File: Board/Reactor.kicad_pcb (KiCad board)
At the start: 2 copper layers, 72.4 x 77.1 mm, 26 parts, among them P1 CONN_02X13, P2 USER_PORT, P3 CONN_01X13, P4 LA_PWR, P5 USB_OTG, P6 DEBUG, U1 usb1232h, U2 PCF8574

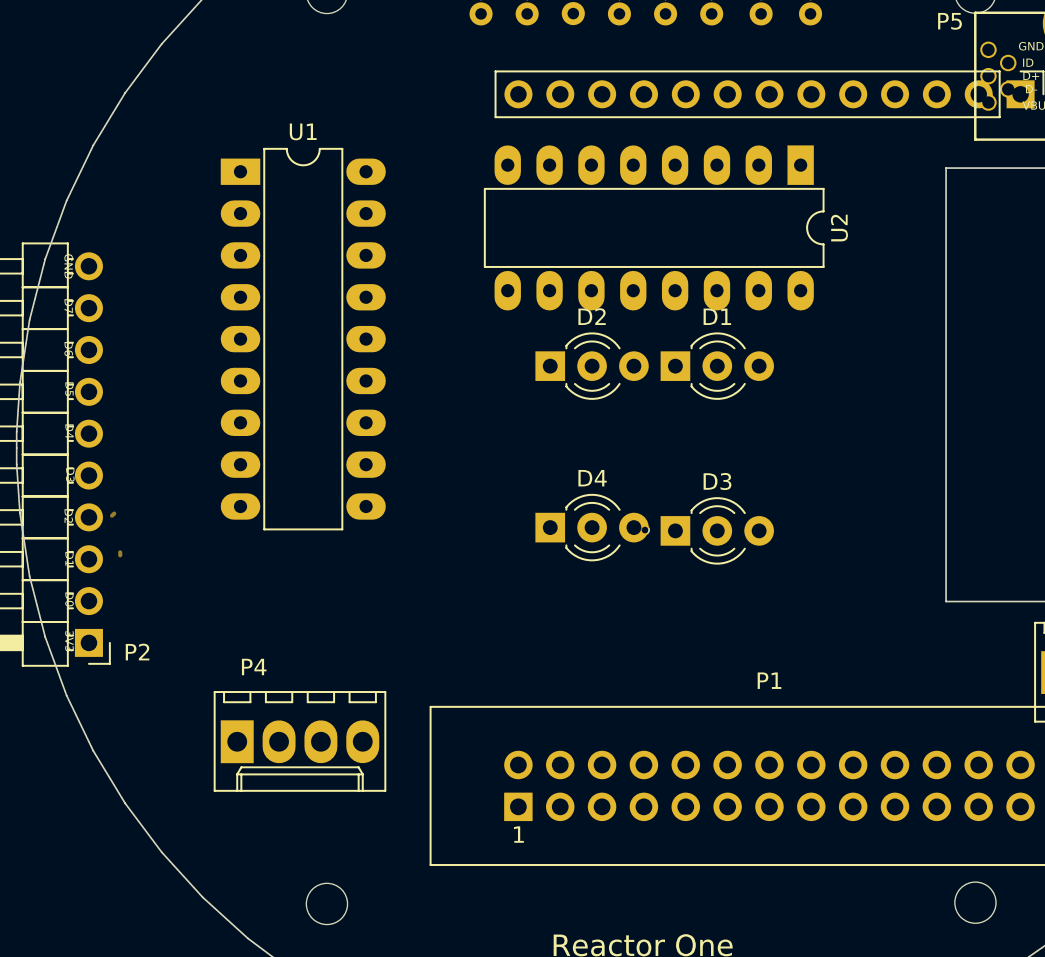
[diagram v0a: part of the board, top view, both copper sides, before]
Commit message: Moved to a template FastSharedBuffer.
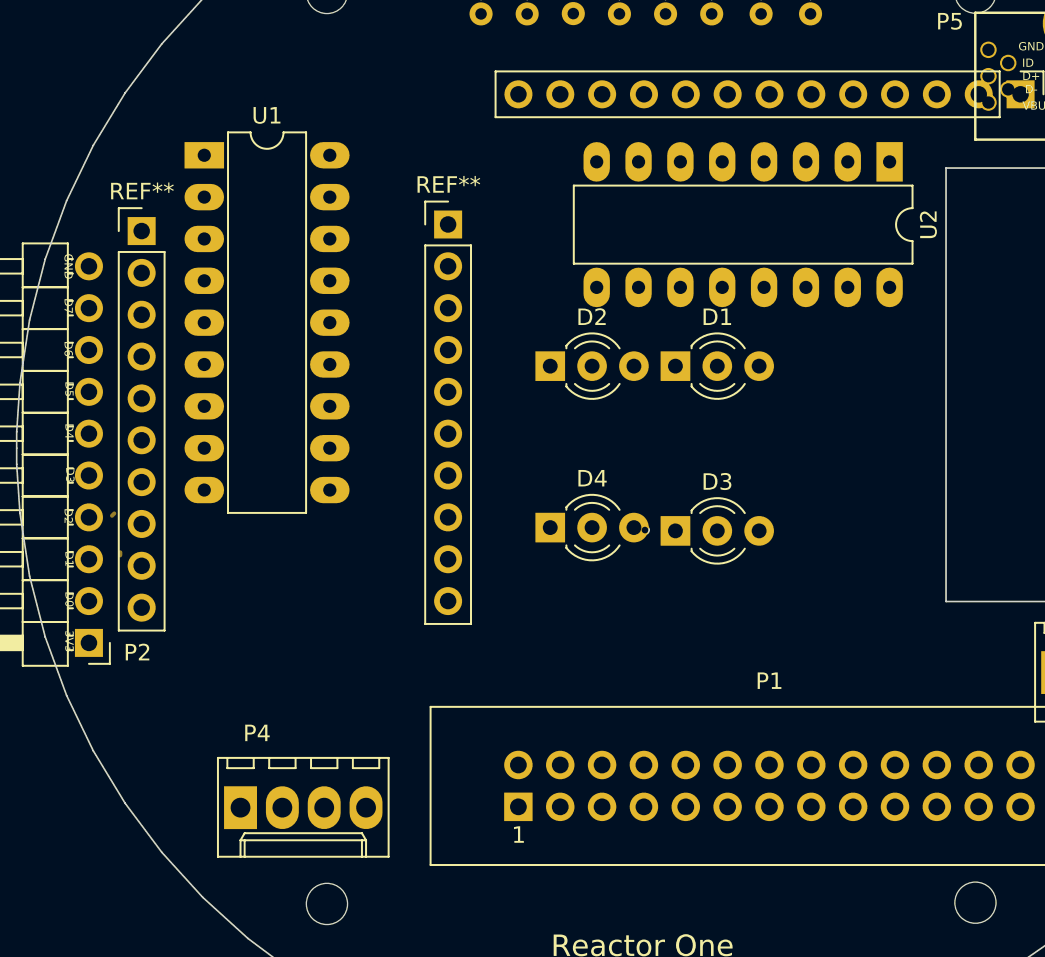
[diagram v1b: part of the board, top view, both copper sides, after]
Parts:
- added REF**: Pin_Header_Straight_1x10_Pitch2.54mm, Pin_Headers_new:Pin_Header_Straight_1x10_Pitch2.54mm, F.Cu at (146.2, 81.9)
- added REF**: Pin_Header_Straight_1x10_Pitch2.54mm, Pin_Headers_new:Pin_Header_Straight_1x10_Pitch2.54mm, F.Cu at (127.6, 82.3)
- moved U2 5.40 mm to (173.0, 78.1)
- moved P4 4.00 mm to (133.6, 117.3)
- moved U1 2.42 mm to (131.4, 77.7)
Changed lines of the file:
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@@
     (tracks 16)
     (zones 0)
-    (modules 26)
+    (modules 28)
     (nets 54)
   )
@@
   )
   (module Connectors_Molex:Molex_KK-6410-04_04x2.54mm_Straight (layer F.Cu)
-    (at 133.39 113.27)
+    (at 133.59 117.27)
     (descr "Connector Headers with Friction Lock, 22-27-2041, http://www.molex.com/pdm_docs/sd/022272021_sd.pdf")
     (tags "connector molex kk_6410 22-27-2041")
@@
   )
   (module Housings_DIP:DIP-18_W7.62mm_LongPads (layer F.Cu)
-    (at 133.59 78.67)
+    (at 131.39 77.67)
     (descr "18-lead dip package, row spacing 7.62 mm (300 mils), LongPads")
     (tags "DIL DIP PDIP 2.54mm 7.62mm 300mil LongPads")
@@
   )
   (module Housings_DIP:DIP-16_W7.62mm_LongPads (layer F.Cu)
-    (at 167.59 78.27 270)
+    (at 172.99 78.07 270)
     (descr "16-lead dip package, row spacing 7.62 mm (300 mils), LongPads")
     (tags "DIL DIP PDIP 2.54mm 7.62mm 300mil LongPads")
@@
     )
   )
-  (gr_line (start 129.99 107.07) (end 129.99 74.87) (angle 90) (layer Cmts.User) (width 0.2))
-  (gr_line (start 144.99 107.07) (end 129.99 107.07) (angle 90) (layer Cmts.User) (width 0.2))
-  (gr_line (start 144.99 74.87) (end 144.99 107.07) (angle 90) (layer Cmts.User) (width 0.2))
-  (gr_line (start 129.99 74.87) (end 144.79 74.87) (angle 90) (layer Cmts.User) (width 0.2))
+  (module Pin_Headers_new:Pin_Header_Straight_1x10_Pitch2.54mm (layer F.Cu)
+    (at 146.19 81.87)
+    (descr "Through hole straight pin header, 1x10, 2.54mm pitch, single row")
+    (tags "Through hole pin header THT 1x10 2.54mm single row")
+    (fp_text reference REF** (at 0 -2.39) (layer F.SilkS)
+      (effects (font (size 1 1) (thickness 0.15)))
+    )
+    (fp_text value Pin_Header_Straight_1x10_Pitch2.54mm (at 0 25.25) (layer F.Fab)
+      (effects (font (size 1 1) (thickness 0.15)))
+    )
+    (fp_line (start -1.27 -1.27) (end -1.27 24.13) (layer F.Fab) (width 0.1))
+    (fp_line (start -1.27 24.13) (end 1.27 24.13) (layer F.Fab) (width 0.1))
+    (fp_line (start 1.27 24.13) (end 1.27 -1.27) (layer F.Fab) (width 0.1))
+    (fp_line (start 1.27 -1.27) (end -1.27 -1.27) (layer F.Fab) (width 0.1))
+    (fp_line (start -1.39 1.27) (end -1.39 24.25) (layer F.SilkS) (width 0.12))
+    (fp_line (start -1.39 24.25) (end 1.39 24.25) (layer F.SilkS) (width 0.12))
+    (fp_line (start 1.39 24.25) (end 1.39 1.27) (layer F.SilkS) (width 0.12))
+    (fp_line (start 1.39 1.27) (end -1.39 1.27) (layer F.SilkS) (width 0.12))
+    (fp_line (start -1.39 0) (end -1.39 -1.39) (layer F.SilkS) (width 0.12))
+    (fp_line (start -1.39 -1.39) (end 0 -1.39) (layer F.SilkS) (width 0.12))
+    (fp_line (start -1.6 -1.6) (end -1.6 24.4) (layer F.CrtYd) (width 0.05))
+    (fp_line (start -1.6 24.4) (end 1.6 24.4) (layer F.CrtYd) (width 0.05))
+    (fp_line (start 1.6 24.4) (end 1.6 -1.6) (layer F.CrtYd) (width 0.05))
+    (fp_line (start 1.6 -1.6) (end -1.6 -1.6) (layer F.CrtYd) (width 0.05))
+    (pad 1 thru_hole rect (at 0 0) (size 1.7 1.7) (drill 1) (layers *.Cu *.Mask))
+    (pad 2 thru_hole oval (at 0 2.54) (size 1.7 1.7) (drill 1) (layers *.Cu *.Mask))
+    (pad 3 thru_hole oval (at 0 5.08) (size 1.7 1.7) (drill 1) (layers *.Cu *.Mask))
+    (pad 4 thru_hole oval (at 0 7.62) (size 1.7 1.7) (drill 1) (layers *.Cu *.Mask))
+    (pad 5 thru_hole oval (at 0 10.16) (size 1.7 1.7) (drill 1) (layers *.Cu *.Mask))
+    (pad 6 thru_hole oval (at 0 12.7) (size 1.7 1.7) (drill 1) (layers *.Cu *.Mask))
+    (pad 7 thru_hole oval (at 0 15.24) (size 1.7 1.7) (drill 1) (layers *.Cu *.Mask))
+    (pad 8 thru_hole oval (at 0 17.78) (size 1.7 1.7) (drill 1) (layers *.Cu *.Mask))
+    (pad 9 thru_hole oval (at 0 20.32) (size 1.7 1.7) (drill 1) (layers *.Cu *.Mask))
+    (pad 10 thru_hole oval (at 0 22.86) (size 1.7 1.7) (drill 1) (layers *.Cu *.Mask))
+    (model Pin_Headers.3dshapes/Pin_Header_Straight_1x10_Pitch2.54mm.wrl
+      (at (xyz 0 -0.45 0))
+      (scale (xyz 1 1 1))
+      (rotate (xyz 0 0 90))
+    )
+  )
+  (module Pin_Headers_new:Pin_Header_Straight_1x10_Pitch2.54mm (layer F.Cu)
+    (at 127.59 82.27)
+    (descr "Through hole straight pin header, 1x10, 2.54mm pitch, single row")
+    (tags "Through hole pin header THT 1x10 2.54mm single row")
+    (fp_text reference REF** (at 0 -2.39) (layer F.SilkS)
+      (effects (font (size 1 1) (thickness 0.15)))
+    )
+    (fp_text value Pin_Header_Straight_1x10_Pitch2.54mm (at 0 25.25) (layer F.Fab)
+      (effects (font (size 1 1) (thickness 0.15)))
+    )
+    (fp_line (start -1.27 -1.27) (end -1.27 24.13) (layer F.Fab) (width 0.1))
+    (fp_line (start -1.27 24.13) (end 1.27 24.13) (layer F.Fab) (width 0.1))
+    (fp_line (start 1.27 24.13) (end 1.27 -1.27) (layer F.Fab) (width 0.1))
+    (fp_line (start 1.27 -1.27) (end -1.27 -1.27) (layer F.Fab) (width 0.1))
+    (fp_line (start -1.39 1.27) (end -1.39 24.25) (layer F.SilkS) (width 0.12))
+    (fp_line (start -1.39 24.25) (end 1.39 24.25) (layer F.SilkS) (width 0.12))
+    (fp_line (start 1.39 24.25) (end 1.39 1.27) (layer F.SilkS) (width 0.12))
+    (fp_line (start 1.39 1.27) (end -1.39 1.27) (layer F.SilkS) (width 0.12))
+    (fp_line (start -1.39 0) (end -1.39 -1.39) (layer F.SilkS) (width 0.12))
+    (fp_line (start -1.39 -1.39) (end 0 -1.39) (layer F.SilkS) (width 0.12))
+    (fp_line (start -1.6 -1.6) (end -1.6 24.4) (layer F.CrtYd) (width 0.05))
+    (fp_line (start -1.6 24.4) (end 1.6 24.4) (layer F.CrtYd) (width 0.05))
+    (fp_line (start 1.6 24.4) (end 1.6 -1.6) (layer F.CrtYd) (width 0.05))
+    (fp_line (start 1.6 -1.6) (end -1.6 -1.6) (layer F.CrtYd) (width 0.05))
+    (pad 1 thru_hole rect (at 0 0) (size 1.7 1.7) (drill 1) (layers *.Cu *.Mask))
+    (pad 2 thru_hole oval (at 0 2.54) (size 1.7 1.7) (drill 1) (layers *.Cu *.Mask))
+    (pad 3 thru_hole oval (at 0 5.08) (size 1.7 1.7) (drill 1) (layers *.Cu *.Mask))
+    (pad 4 thru_hole oval (at 0 7.62) (size 1.7 1.7) (drill 1) (layers *.Cu *.Mask))
+    (pad 5 thru_hole oval (at 0 10.16) (size 1.7 1.7) (drill 1) (layers *.Cu *.Mask))
+    (pad 6 thru_hole oval (at 0 12.7) (size 1.7 1.7) (drill 1) (layers *.Cu *.Mask))
+    (pad 7 thru_hole oval (at 0 15.24) (size 1.7 1.7) (drill 1) (layers *.Cu *.Mask))
+    (pad 8 thru_hole oval (at 0 17.78) (size 1.7 1.7) (drill 1) (layers *.Cu *.Mask))
+    (pad 9 thru_hole oval (at 0 20.32) (size 1.7 1.7) (drill 1) (layers *.Cu *.Mask))
+    (pad 10 thru_hole oval (at 0 22.86) (size 1.7 1.7) (drill 1) (layers *.Cu *.Mask))
+    (model Pin_Headers.3dshapes/Pin_Header_Straight_1x10_Pitch2.54mm.wrl
+      (at (xyz 0 -0.45 0))
+      (scale (xyz 1 1 1))
+      (rotate (xyz 0 0 90))
+    )
+  )
+  (gr_line (start 148.99 74.67) (end 126.59 74.67) (angle 90) (layer Cmts.User) (width 0.2))
+  (gr_line (start 148.99 113.07) (end 148.99 74.67) (angle 90) (layer Cmts.User) (width 0.2))
+  (gr_line (start 126.59 113.07) (end 148.99 113.07) (angle 90) (layer Cmts.User) (width 0.2))
+  (gr_line (start 126.59 74.67) (end 126.59 113.07) (angle 90) (layer Cmts.User) (width 0.2))
   (gr_text CLK (at 178.49 118.72) (layer B.SilkS)
     (effects (font (size 0.5 0.5) (thickness 0.1)) (justify mirror))

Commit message: - board laid out (draft).
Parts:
- removed ? (x4): , Mounting_Holes:MountingHole_2.5mm
- removed P4: LA_PWR, Connectors_Molex:Molex_KK-6410-04_04x2.54mm_Straight
- removed REF** (x2): MountingHole_2.2mm_M2_DIN965_Pad, Mounting_Holes:MountingHole_2.2mm_M2_DIN965_Pad
- removed REF** (x2): Pin_Header_Straight_1x10_Pitch2.54mm, Pin_Headers_new:Pin_Header_Straight_1x10_Pitch2.54mm
- D1, D2, D3, D4: value LED_Dual_AAC -> LED_Dual_CAC; footprint LEDs_new:LED_D3.0mm-3 -> sip:SIP3
- U1: value usb1232h -> AdafruitFT232H; footprint Housings_DIP:DIP-18_W7.62mm_LongPads -> ReactorProject:AdafruitFT232h
- moved R2 41.9 mm to (162.0, 102.9), turned to 0 degrees
- moved R4 41.8 mm to (151.0, 103.3), turned to 0 degrees
- moved U1 41.3 mm to (149.8, 114.7), turned to 90 degrees
- moved R5 37.8 mm to (169.6, 97.9), turned to 180 degrees
- moved R7 37.0 mm to (158.6, 97.9), turned to 180 degrees
- moved R3 31.9 mm to (150.8, 93.3), turned to 0 degrees
- moved R1 31.8 mm to (162.2, 93.3), turned to 0 degrees
- moved R8 26.5 mm to (158.6, 87.9), turned to 180 degrees
- moved R6 20.5 mm to (162.0, 87.9), turned to 0 degrees
- moved U2 17.6 mm to (167.8, 61.3)
- moved P5 8.44 mm to (173.4, 67.9)
- moved D2 2.60 mm to (155.0, 90.5)
- moved D1 2.60 mm to (162.6, 90.5)
- moved D4 2.41 mm to (154.8, 100.5)
- moved D3 2.40 mm to (162.4, 100.5)
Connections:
- net /PA19 renamed Net-(P1-Pad16)
- D1 pad 2: Net-(D1-Pad2) -> /3v3
- D1 pad 3: +5V -> Net-(D1-Pad3)
- D2 pad 2: Net-(D2-Pad2) -> /3v3
- D2 pad 3: +5V -> Net-(D2-Pad3)
- D3 pad 2: Net-(D3-Pad2) -> /3v3
- D3 pad 3: +5V -> Net-(D3-Pad3)
- D4 pad 2: Net-(D4-Pad2) -> /3v3
- D4 pad 3: +5V -> Net-(D4-Pad3)
- P1 pad 12: /3v3 -> /D7
- P1 pad 18: /3v3 -> /D7
- P1 pad 21: /3v3 -> /D6
- P1 pad 25: +5V -> /GND
- P1 pad 7: /3v3 -> /D6
- P2 pad 1: +5V -> /GND
- P2 pad 8: /3v3 -> /D6
- P2 pad 9: /3v3 -> /D7
- P3 pad 1: +5V -> /5V
- P3 pad 2: +5V -> /GND
- P5 pad 1: +5V -> /5V
- P5 pad 5: +5V -> /GND
- P6 pad 1: +5V -> Net-(P6-Pad1)
- R1 pad 1: Net-(R1-Pad1) -> Net-(D1-Pad3)
- R1 pad 2: Net-(D3-Pad1) -> Net-(R1-Pad2)
- R2 pad 1: Net-(R2-Pad1) -> Net-(D3-Pad1)
- R2 pad 2: Net-(D3-Pad2) -> Net-(R2-Pad2)
- R3 pad 1: Net-(R3-Pad1) -> Net-(D2-Pad1)
- R3 pad 2: Net-(D4-Pad1) -> Net-(R3-Pad2)
- R4 pad 1: Net-(R4-Pad1) -> Net-(D4-Pad1)
- R4 pad 2: Net-(D4-Pad2) -> Net-(R4-Pad2)
- R5 pad 1: Net-(R5-Pad1) -> Net-(D3-Pad3)
- R5 pad 2: Net-(D1-Pad1) -> Net-(R5-Pad2)
- R6 pad 1: Net-(R6-Pad1) -> Net-(D1-Pad1)
- R6 pad 2: Net-(D1-Pad2) -> Net-(R6-Pad2)
- R7 pad 1: Net-(R7-Pad1) -> Net-(D4-Pad3)
- R7 pad 2: Net-(D2-Pad1) -> Net-(R7-Pad2)
- R8 pad 1: Net-(R8-Pad1) -> Net-(D2-Pad3)
- R8 pad 2: Net-(D2-Pad2) -> Net-(R8-Pad2)
- U1 pad 1: +5V -> Net-(U1-Pad1)
- U1 pad 10: +5V -> Net-(U1-Pad10)
- U1 pad 11: +5V -> /D7
- U1 pad 12: +5V -> /D6
- U1 pad 13: /3v3 -> /D5
- U1 pad 14: Net-(U1-Pad14) -> /D4
- U1 pad 15: Net-(U1-Pad15) -> /D3
- U1 pad 16: /D1 -> /D2
- U1 pad 17: /D4 -> /D1
- U1 pad 2: /D2 -> Net-(U1-Pad2)
- U1 pad 3: /3v3 -> Net-(U1-Pad3)
- U1 pad 4: /D5 -> Net-(U1-Pad4)
- U1 pad 5: /D3 -> Net-(U1-Pad5)
- U1 pad 6: +5V -> Net-(U1-Pad6)
- U1 pad 7: +5V -> Net-(U1-Pad7)
- U1 pad 8: +5V -> Net-(U1-Pad8)
- U1 pad 9: +5V -> Net-(U1-Pad9)
- U2 pad 1: +5V -> /GND
- U2 pad 10: Net-(R7-Pad1) -> Net-(R2-Pad2)
- U2 pad 11: Net-(R6-Pad1) -> Net-(R7-Pad2)
- U2 pad 12: Net-(R5-Pad1) -> Net-(R4-Pad2)
- U2 pad 16: +3V3 -> /3v3
- U2 pad 2: +5V -> /GND
- U2 pad 3: +5V -> /GND
- U2 pad 4: Net-(R4-Pad1) -> Net-(R1-Pad2)
- U2 pad 5: Net-(R3-Pad1) -> Net-(R6-Pad2)
- U2 pad 6: Net-(R2-Pad1) -> Net-(R8-Pad2)
- U2 pad 7: Net-(R1-Pad1) -> Net-(R3-Pad2)
- U2 pad 8: +5V -> /GND
- U2 pad 9: Net-(R8-Pad1) -> Net-(R5-Pad2)
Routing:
- net /GND: track 0.00 -> 170.1 mm, vias 0 -> 1
- net /D0: track 0.00 -> 125.3 mm, vias 0 -> 2
- net /D5: track 0.00 -> 115.6 mm, vias 0 -> 4
- net /3v3: track 0.83 -> 115.7 mm, vias 0 -> 5
- net /D4: track 0.00 -> 105.9 mm, vias 0 -> 1
- net /USBDM2: track 0.00 -> 103.8 mm
- net /USBDP2: track 0.00 -> 102.9 mm
- net /D6: track 0.00 -> 99.0 mm, vias 0 -> 1
- net /D2: track 0.00 -> 98.2 mm, vias 0 -> 1
- net /D7: track 0.00 -> 89.5 mm, vias 0 -> 4
- net /D1: track 0.25 -> 87.5 mm, vias 0 -> 1
- net /D3: track 0.00 -> 83.2 mm, vias 0 -> 1
- net /PG6: track 0.59 -> 65.9 mm, vias 0 -> 2
- net /PG7: track 0.46 -> 63.8 mm, vias 0 -> 2
- net Net-(R2-Pad2): track 0.00 -> 49.0 mm
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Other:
- board text added: "(March 2017)"
- board text removed: "(Jan 2017)"
